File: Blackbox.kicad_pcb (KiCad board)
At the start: 2 copper layers, 42 parts, among them CN1 SM04B-SRSS-TB (LF)(SN), U1 SN65HVD232DR, U2 STM32G0B1CCT6, U3 BM06B-SRSS-TB(LF)(SN), X2 DSX321G-48M

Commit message: Update schematic and PCB with latest changes
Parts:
- removed C6: 100nF, EasyEDA:C0603
- removed D14, D15, D22: 0603ESDA-05N, EasyEDA:D0603-BI
- moved C2 60.3 mm to (196.5, 113.0), turned to -90 degrees
- moved X2 57.1 mm to (189.0, 113.5), turned to 90 degrees
- moved D23 55.8 mm to (197.4, 95.5)
- moved C8 54.2 mm to (197.5, 93.0)
- moved U3 50.4 mm to (112.0, 128.5), turned to -90 degrees
- moved CN1 50.3 mm to (203.0, 100.5), turned to 90 degrees
- moved D13 49.1 mm to (186.5, 92.0), turned to 90 degrees
- moved C1 45.7 mm to (182.0, 113.0), turned to 90 degrees
- moved Card1 43.3 mm to (95.5, 99.0), turned to -90 degrees
- moved D17 43.0 mm to (103.8, 89.7), turned to 90 degrees
- moved C3 41.8 mm to (106.8, 97.5), turned to 90 degrees
- moved D16 39.7 mm to (182.5, 92.0), turned to 90 degrees
- moved C5 39.7 mm to (120.5, 136.0), turned to 180 degrees
- moved D12 36.2 mm to (175.5, 98.4), turned to -90 degrees
- moved D10 34.8 mm to (109.3, 89.5), turned to 90 degrees
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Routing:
- net VDD: track 0.00 -> 1.91 mm, vias 0 -> 1
- net GND: track 0.00 -> 1.81 mm, vias 0 -> 1

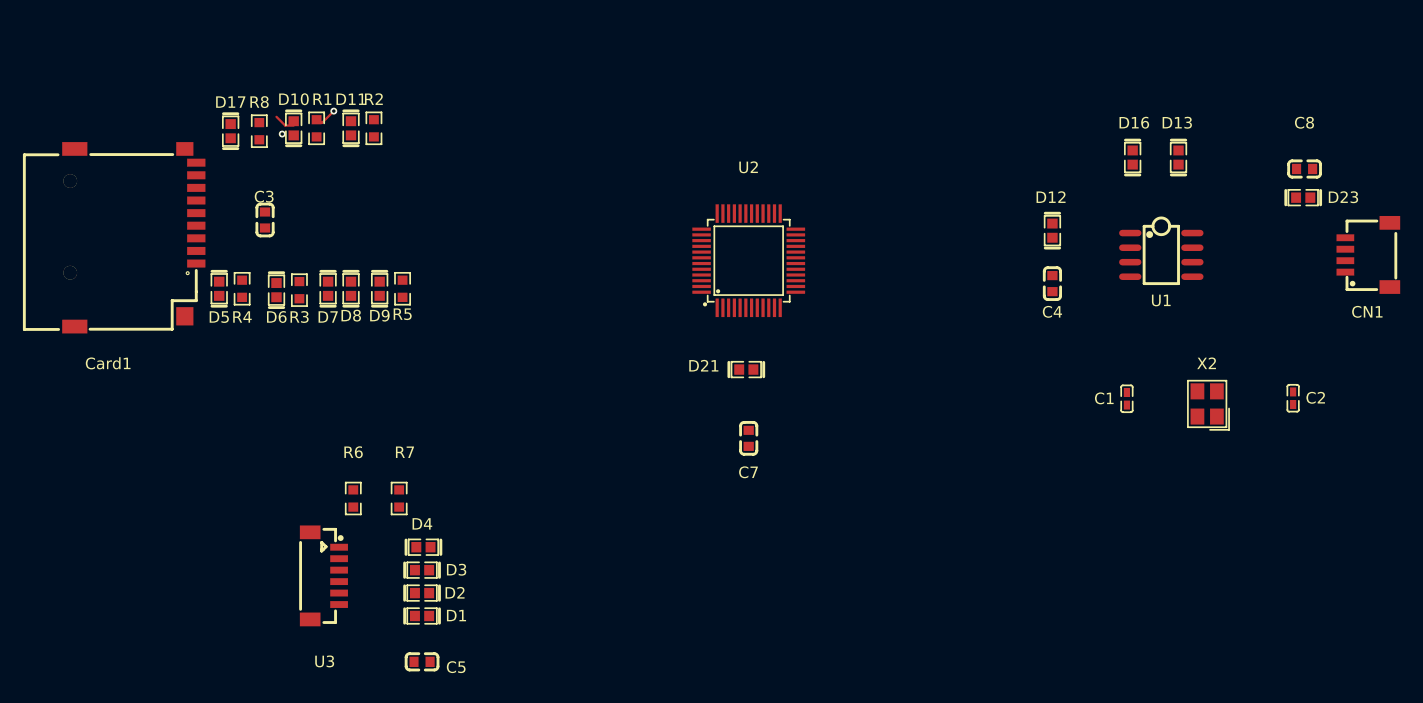
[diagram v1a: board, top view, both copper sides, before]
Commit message: The PCB connections are completed
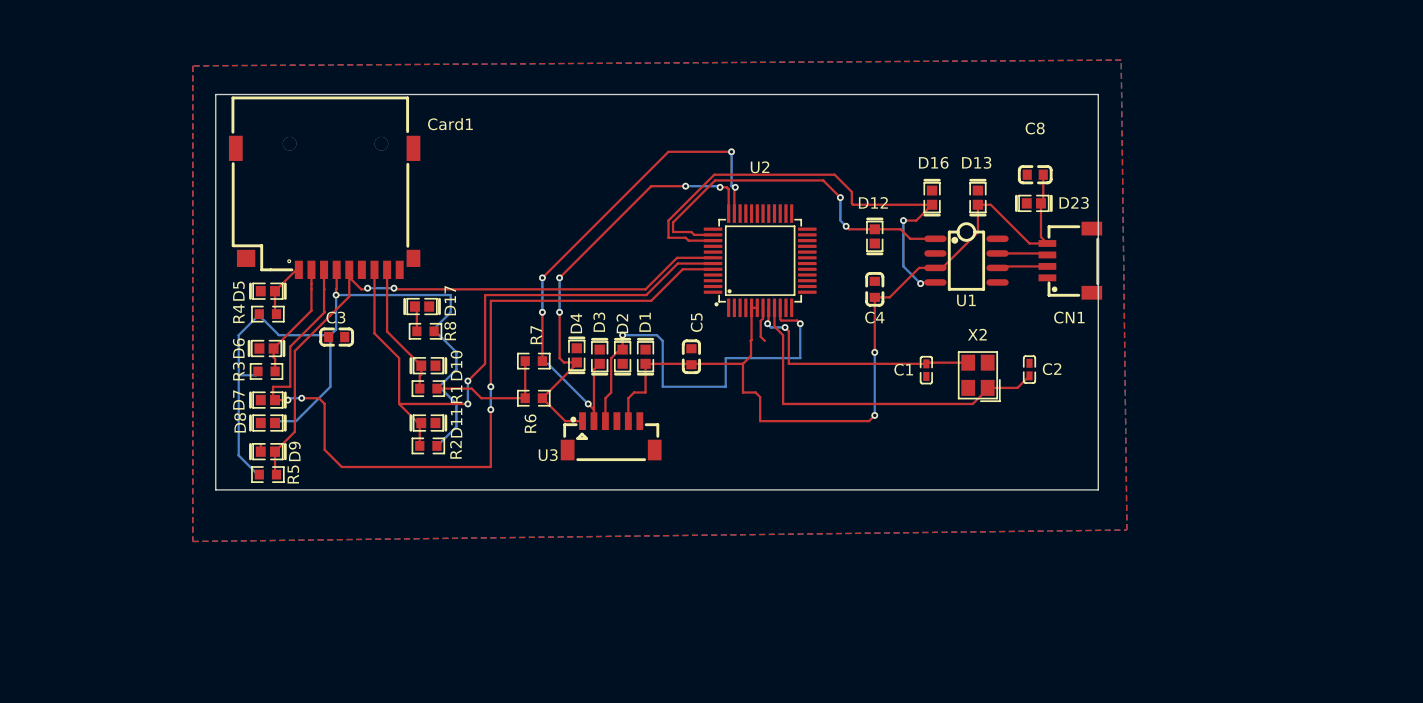
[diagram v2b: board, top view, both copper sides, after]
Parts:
- removed C7: 100nF, EasyEDA:C0603
- removed D21: 0603ESDA-05N, EasyEDA:D0603-BI
- moved C5 35.5 mm to (144.0, 109.4), turned to -90 degrees
- moved D1 29.9 mm to (140.0, 109.4), turned to -90 degrees
- moved R2 28.1 mm to (121.0, 117.2), turned to 180 degrees
- moved U3 27.8 mm to (137.0, 116.3), turned to 0 degrees
- moved D2 27.0 mm to (138.0, 109.4), turned to 90 degrees
- moved D11 26.6 mm to (121.0, 115.2), turned to 0 degrees
- moved CN1 26.0 mm to (177.0, 101.0)
- moved R1 24.7 mm to (121.0, 112.2), turned to 180 degrees
- moved D3 24.2 mm to (136.0, 109.4), turned to -90 degrees
- moved D10 23.8 mm to (121.0, 110.2), turned to 0 degrees
- moved C8 23.5 mm to (174.0, 93.5)
- moved D23 23.5 mm to (173.9, 96.0)
- moved C2 23.1 mm to (173.5, 110.5)
- moved R8 22.7 mm to (120.8, 107.2), turned to 180 degrees
- moved D17 22.6 mm to (120.5, 105.0), turned to 0 degrees
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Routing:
- net VDD: track 1.91 -> 154.4 mm, vias 1 -> 3
- net CMD: track 0.00 -> 73.0 mm, vias 0 -> 4
- net CLK: track 0.00 -> 55.0 mm, vias 0 -> 2
- net Dat0: track 0.00 -> 54.4 mm, vias 0 -> 2
- net SWDIO: track 0.00 -> 46.4 mm, vias 0 -> 5
- net RX: track 0.00 -> 42.3 mm, vias 0 -> 2
- net SWCLK: track 0.00 -> 37.7 mm, vias 0 -> 4
- net NRST: track 0.00 -> 36.4 mm, vias 0 -> 2
- net TX: track 0.00 -> 32.1 mm, vias 0 -> 2
- net Net-(U2-PF1-OSC_OUT): track 0.00 -> 31.3 mm
- net Net-(U2-PF0-OSC_IN): track 0.00 -> 22.1 mm, vias 0 -> 2
- net Dat1: track 0.00 -> 11.7 mm
- net Dat3: track 0.00 -> 10.3 mm
- net Dat2: track 0.00 -> 4.91 mm
- net Net-(U1-CANL): track 0.00 -> 4.40 mm
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- added copper zone on B.Cu, net GND
- added copper zone on F.Cu, net GND
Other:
- board outline added: 77 x 34.5 mm

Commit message: updated pcb
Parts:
- added C6: 100nF, EasyEDA:C0603, F.Cu at (144.0, 113.0)
- added D22: 0603ESDA-05N, EasyEDA:D0603-BI, F.Cu at (144.0, 116.0)
- moved R6 28.2 mm to (152.5, 95.6), turned to 90 degrees
- moved U3 27.5 mm to (145.0, 90.0), turned to 180 degrees
- moved C2 23.5 mm to (150.0, 112.0), turned to 0 degrees
- moved R5 23.3 mm to (125.5, 105.5), turned to 90 degrees
- moved D8 23.0 mm to (125.5, 101.5), turned to -90 degrees
- moved R4 22.4 mm to (125.5, 118.4), turned to 90 degrees
- moved R7 22.4 mm to (147.5, 95.5), turned to 90 degrees
- moved D5 21.7 mm to (123.0, 118.4), turned to 90 degrees
- moved D4 21.5 mm to (150.5, 95.5), turned to 90 degrees
- moved D9 20.1 mm to (123.0, 105.5), turned to 90 degrees
- moved R2 19.8 mm to (125.5, 97.9), turned to -90 degrees
- moved R1 18.8 mm to (125.5, 93.9), turned to -90 degrees
- moved R3 18.8 mm to (125.5, 113.5), turned to 90 degrees
- moved R8 18.3 mm to (125.5, 89.5), turned to -90 degrees
- moved D11 17.4 mm to (123.0, 97.9), turned to 90 degrees
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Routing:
- net VDD: track 154.4 -> 0.00 mm, vias 3 -> 0
- net CMD: track 73.0 -> 28.6 mm, vias 4 -> 0
- net CLK: track 55.0 -> 25.1 mm, vias 2 -> 0
- net SWDIO: track 46.4 -> 16.6 mm, vias 5 -> 0
- net Dat0: track 54.4 -> 30.5 mm
- net Net-(U2-PF1-OSC_OUT): track 31.3 -> 10.2 mm
- net SWCLK: track 37.7 -> 20.7 mm, vias 4 -> 2
- net Dat2: track 4.91 -> 19.5 mm
- net RX: track 42.3 -> 31.8 mm
- net CD: track 2.23 -> 12.4 mm
- net Net-(U2-PF0-OSC_IN): track 22.1 -> 16.3 mm
- net Dat1: track 11.7 -> 6.48 mm
- net Dat3: track 10.3 -> 15.0 mm
- net GND: track 3.96 -> 0.00 mm
- net Net-(U1-CANL): track 4.40 -> 6.03 mm
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- added copper zone on In1.Cu, net VDD
- removed copper zone on B.Cu, net GND
- removed copper zone on F.Cu, net GND
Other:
- copper layers 2 -> 4

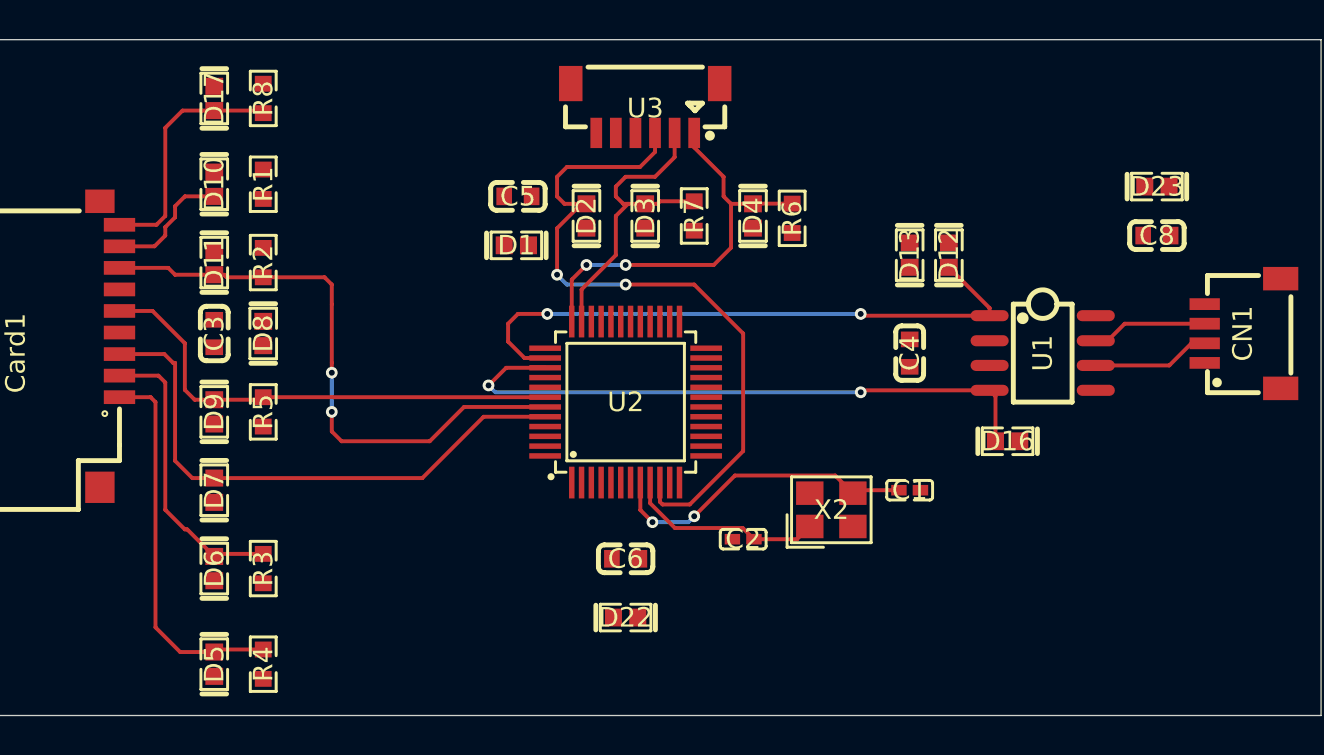
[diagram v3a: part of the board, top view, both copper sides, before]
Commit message: Updated pcb, only mountung holes left
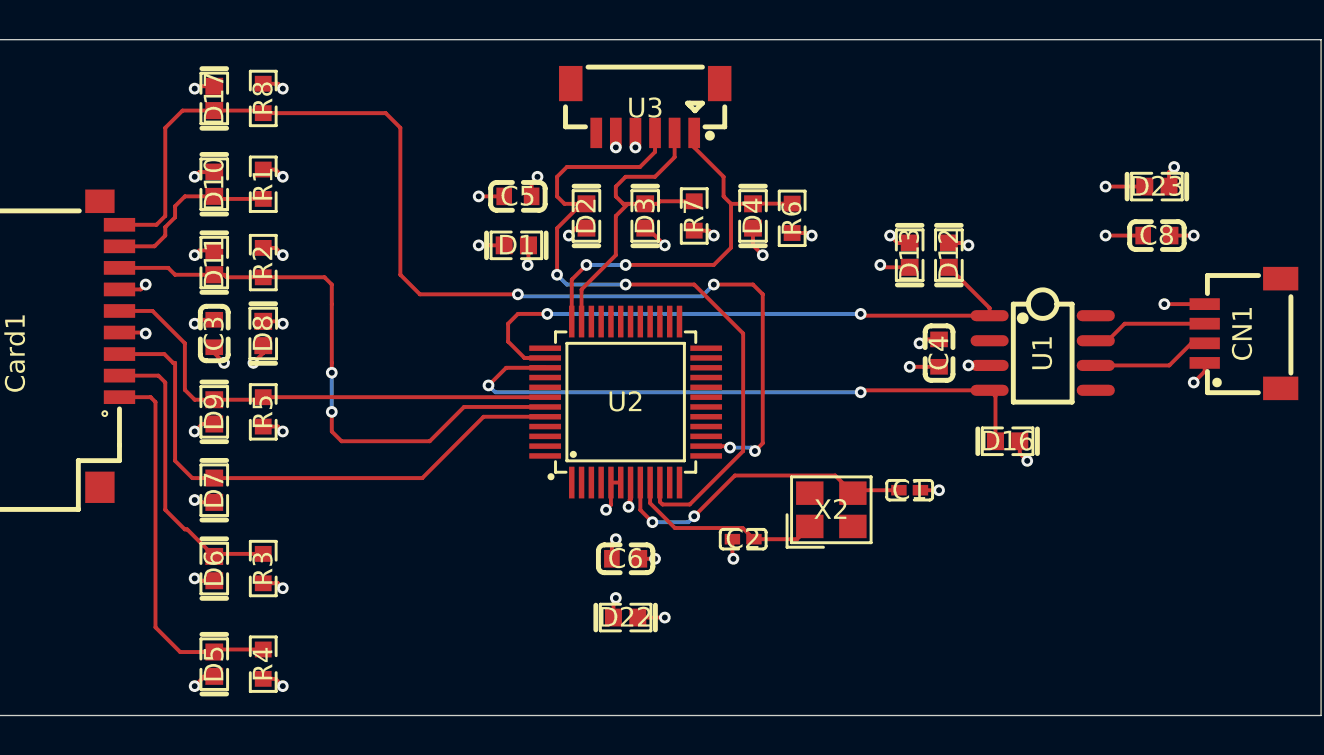
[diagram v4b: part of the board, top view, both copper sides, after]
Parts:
- moved C4 1.50 mm to (160.0, 102.5)
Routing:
- net CD: track 12.4 -> 57.4 mm, vias 0 -> 4
- net GND: track 0.00 -> 32.9 mm, vias 0 -> 28
- net VDD: track 0.00 -> 29.0 mm, vias 0 -> 23
- net Dat1: track 6.48 -> 9.03 mm
- added copper zone on In2.Cu, net GND

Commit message: new pcb design
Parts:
- moved D23 4.37 mm to (169.9, 98.2), turned to -90 degrees
- moved C3 3.16 mm to (120.0, 100.5)
- moved D8 3.16 mm to (122.5, 100.5)
- moved C8 2.14 mm to (172.4, 98.2), turned to -90 degrees
- moved C6 2.06 mm to (143.5, 111.0)
- moved D22 2.06 mm to (143.5, 114.0)
- moved D11 0.76 mm to (123.0, 97.1)
- moved R2 0.76 mm to (125.5, 97.1)
- moved C4 0.50 mm to (160.5, 102.5)
- moved D10 0.38 mm to (123.0, 93.5)
- moved R1 0.38 mm to (125.5, 93.5)
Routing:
- net VDD: track 29.0 -> 38.0 mm, vias 23 -> 16
- net GND: track 32.9 -> 41.1 mm, vias 28 -> 23
- net CLK: track 25.1 -> 24.8 mm, vias 0 -> 2

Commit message: Updated PCB
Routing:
- net GND: track 41.1 -> 43.8 mm
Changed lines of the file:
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@@
-	)
-	(segment
-		(start 161.38 96.88)
-		(end 161.5 97)
-		(width 0.2)
-		(layer "F.Cu")
-		(net 2)
 	)
 	(segment
@@
 	)
 	(segment
-		(start 169.18 97.58)
-		(end 168.92 97.32)
+		(start 168.5 97)
+		(end 168.6 97)
 		(width 0.2)
 		(layer "F.Cu")
@@
 	)
 	(segment
-		(start 159.2 101.8)
-		(end 159 102)
+		(start 162 96.26)
+		(end 161.38 96.88)
+		(width 0.2)
+		(layer "F.Cu")
+		(net 2)
+	)
+	(segment
+		(start 158.9 101.5)
+		(end 159.2 101.8)
 		(width 0.2)
 		(layer "F.Cu")
@@
 	)
 	(segment
+		(start 161.38 96.88)
+		(end 160.5 96.88)
+		(width 0.2)
+		(layer "F.Cu")
+		(net 2)
+	)
+	(segment
 		(start 120.38 99.88)
 		(end 122.5 99.88)
@@
 	)
 	(segment
+		(start 168.6 97)
+		(end 169.18 97.58)
+		(width 0.2)
+		(layer "F.Cu")
+		(net 2)
+	)
+	(segment
 		(start 173.56 103)
 		(end 173.56 103.44)
@@
 	)
 	(segment
-		(start 157.88 96.88)
-		(end 157.5 96.5)
-		(width 0.2)
-		(layer "F.Cu")
-		(net 2)
-	)
-	(segment
 		(start 144.2 113.92)
 		(end 144.12 114)
@@
 	)
 	(segment
+		(start 162 96)
+		(end 162 96.26)
+		(width 0.2)
+		(layer "F.Cu")
+		(net 2)
+	)
+	(segment
 		(start 144.5 91.26)
 		(end 144.5 92)
@@
 	)
 	(segment
-		(start 160.5 96.88)
-		(end 161.38 96.88)
-		(width 0.2)
-		(layer "F.Cu")
-		(net 2)
-	)
-	(segment
 		(start 122.12 88.88)
 		(end 122 89)
@@
 	)
 	(segment
-		(start 160 101.8)
-		(end 159.2 101.8)
+		(start 157 96)
+		(end 157.88 96.88)
 		(width 0.2)
 		(layer "F.Cu")
@@
 	)
 	(segment
-		(start 169.92 97.58)
-		(end 169.18 97.58)
-		(width 0.2)
-		(layer "F.Cu")
-		(net 2)
-	)
-	(segment
 		(start 122.12 114.12)
 		(end 122 114)
@@
 	)
 	(segment
-		(start 158.5 96.88)
-		(end 157.88 96.88)
-		(width 0.2)
-		(layer "F.Cu")
-		(net 2)
-	)
-	(segment
 		(start 144.12 114)
 		(end 144.12 115.38)
@@
 	)
 	(segment
+		(start 157.88 96.88)
+		(end 158.5 96.88)
+		(width 0.2)
+		(layer "F.Cu")
+		(net 2)
+	)
+	(segment
+		(start 158.5 101.5)
+		(end 158.9 101.5)
+		(width 0.2)
+		(layer "F.Cu")
+		(net 2)
+	)
+	(segment
 		(start 144.25 110.95)
 		(end 144.2 111)
@@
 	)
 	(segment
+		(start 169.18 97.58)
+		(end 169.92 97.58)
+		(width 0.2)
+		(layer "F.Cu")
+		(net 2)
+	)
+	(segment
+		(start 159.2 101.8)
+		(end 160 101.8)
+		(width 0.2)
+		(layer "F.Cu")
+		(net 2)
+	)
+	(segment
 		(start 172.42 97.5)
 		(end 170 97.5)
@@
 	)
 	(via
-		(at 157.5 96.5)
+		(at 157 96)
 		(size 0.6)
 		(drill 0.3)
@@
 	)
 	(via
-		(at 159 102)
+		(at 158.5 101.5)
 		(size 0.6)
 		(drill 0.3)
@@
 	)
 	(via
-		(at 161.5 97)
+		(at 162 96)
 		(size 0.6)
 		(drill 0.3)
@@
 	)
 	(via
-		(at 168.92 97.32)
-		(size 0.6)
-		(drill 0.3)
+		(at 168.5 97)
+		(size 0.6)
+		(drill 0.3)

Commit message: PCB update
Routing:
- net RX: track 31.8 -> 33.3 mm
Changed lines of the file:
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@@
+	)
+	(segment
+		(start 136.5 104)
+		(end 136.5 103.5)
+		(width 0.2)
+		(layer "F.Cu")
+		(net 23)
+	)
+	(segment
+		(start 136.5 103.5)
+		(end 137 103)
+		(width 0.2)
+		(layer "F.Cu")
+		(net 23)
 	)
 	(segment
 		(start 162.88 104.7)
 		(end 162.58 104.4)
+		(width 0.2)
+		(layer "F.Cu")
+		(net 23)
+	)
+	(segment
+		(start 137 103)
+		(end 138.25 103)
 		(width 0.2)
 		(layer "F.Cu")
@@
 	)
 	(segment
-		(start 137 104.15)
-		(end 137.9 103.25)
+		(start 138.25 103)
+		(end 138.5 103.25)
 		(width 0.2)
 		(layer "F.Cu")
@@
 	)
 	(segment
-		(start 137.9 103.25)
+		(start 138.5 103.25)
 		(end 139.89 103.25)
 		(width 0.2)
@@
 	)
 	(via
-		(at 137 104.15)
+		(at 136.5 104)
 		(size 0.6)
 		(drill 0.3)
@@
 	(segment
 		(start 137.35 104.5)
-		(end 137 104.15)
+		(end 137 104.5)
 		(width 0.2)
 		(layer "B.Cu")
@@
 	)
 	(segment
-		(start 156 104.5)
-		(end 137.35 104.5)
+		(start 137 104.5)
+		(end 136.5 104)
 		(width 0.2)
 		(layer "B.Cu")
+		(net 23)
+	)
+	(segment
+		(start 137.35 104.5)
+		(end 156 104.5)
+		(width 0.2)
+		(layer "B.Cu")

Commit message: Final PCB Design
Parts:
- added G***: LOGO, LOGO, F.Cu at (163.0, 116.5)
- added REF**: MountingHole_2.2mm_M2_Pad_Via, MountingHole:MountingHole_2.2mm_M2_Pad_Via, F.Cu at (173.5, 117.5)
- added REF**: MountingHole_2.2mm_M2_Pad_Via, MountingHole:MountingHole_2.2mm_M2_Pad_Via, F.Cu at (173.5, 90.0)
- added REF**: MountingHole_2.2mm_M2_Pad_Via, MountingHole:MountingHole_2.2mm_M2_Pad_Via, F.Cu at (107.5, 117.0)
- added REF**: MountingHole_2.2mm_M2_Pad_Via, MountingHole:MountingHole_2.2mm_M2_Pad_Via, F.Cu at (107.5, 90.5)
- moved D22 1.12 mm to (143.0, 113.0)
- moved C6 0.30 mm to (143.2, 111.0)
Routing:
- net GND: track 43.8 -> 48.0 mm
- net VDD: track 38.0 -> 40.6 mm
